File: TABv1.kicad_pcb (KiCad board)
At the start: 4 copper layers, 90 x 45 mm, 136 parts, among them IC1 TPS630702RNMR, J10 Conn_02x03_Odd_Even, J2 Conn_01x03_Socket, J3 Conn_01x03_Socket, J4 Conn_Coaxial, J5 Conn_02x06_Counter_Clockwise, J7 503398-1892, J8 1053141104, J9 Conn_02x03_Odd_Even, Q1 MJD44H11T4G, Q10 PJM09P30DF, Q11 PJM09P30DF, Q12 PJM09P30DF, Q2 DMN2040U, Q3 DMN2040U, Q4 BC817-25,215, Q5 DMN2040U, Q6 DMN2040U, Q7 DMN2040U, SW1 BOOTSEL, SW2 RESET, U1 RP2350B-QFN80, U10 RAK3172, U11 LPS22DF, U2 W25Q128JVS, U4 LSM6DSV80XTR, U5 LSM6DSV80XTR, U7 LM334M, U8 LIS2MDL, Y1 12MHz

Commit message: Tentativo di Sbroglio
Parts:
- removed FPC1: WL0540013-120R-001, easyeda2kicad:CONN-SMD_12P-WL0540013-120R-001
- removed the J5 at (87.6, 47.2)
- removed the J5 at (122.9, 47.2)
- added H5: MountingHole, MountingHole:MountingHole_3.2mm_M3, F.Cu at (131.0, 74.0)
- added H6: MountingHole, MountingHole:MountingHole_3.2mm_M3, F.Cu at (86.5, 38.0)
- added J11: Conn_02x06_Counter_Clockwise, Connector_PinHeader_2.54mm:PinHeader_2x06_P2.54mm_Vertical, B.Cu at (87.6, 47.2)
- added J6: Conn_02x06_Counter_Clockwise, Connector_PinHeader_2.54mm:PinHeader_2x06_P2.54mm_Vertical, B.Cu at (122.9, 47.2)
- BT1, C37, D8, JP1, R26, R39, R9: moved to F.Cu
- C10, C11, C12, C15, C5, C9, D5, D6, D7, J7, R7, SW1, SW2, USB1: moved to B.Cu
- moved R39 141.3 mm to (22.3, 133.1), turned to 0 degrees
- moved C37 138.9 mm to (22.3, 130.6)
- moved D8 137.3 mm to (26.7, 130.6), turned to 0 degrees
- moved BT1 135.5 mm to (29.4, 125.1), turned to 0 degrees
- moved JP1 128.3 mm to (31.1, 131.1), turned to 0 degrees
- moved R9 84.3 mm to (126.3, 60.3), turned to 0 degrees
- moved R26 82.8 mm to (126.3, 58.7), turned to 0 degrees
- moved G*** 63.2 mm to (174.4, 88.9)
- moved D10 62.8 mm to (38.8, 106.0)
- moved D11 62.8 mm to (38.8, 107.7)
- moved D9 62.8 mm to (38.8, 104.2)
- moved RN1 62.8 mm to (38.1, 115.0)
- moved C39 56.3 mm to (66.1, 104.7)
- moved C40 56.3 mm to (66.1, 103.2)
- moved C5 26.2 mm to (114.6, 59.6), turned to 180 degrees
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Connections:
- J7 pad 3: Net-(J7-CMD) -> /microSD/_CMD
- J7 pad 5: Net-(J7-CLK) -> /microSD/_CLK
- J7 pad 7: Net-(J7-DAT0) -> /microSD/_DAT0
- RN6 pad 1: Net-(J7-CMD) -> unconnected-(RN6-R1.1-Pad1)
- RN6 pad 2: unconnected-(RN6-R2.1-Pad2) -> /microSD/_CMD
- RN6 pad 7: unconnected-(RN6-R2.2-Pad7) -> +3V3
- RN7 pad 1: /microSD/_DAT3 -> unconnected-(RN7-R1.1-Pad1)
- RN7 pad 2: unconnected-(RN7-R2.1-Pad2) -> /SD_DAT1
- RN7 pad 3: Net-(J7-CMD) -> /SD_DAT0
- RN7 pad 4: /microSD/_DAT2 -> /SD_CLK
- RN7 pad 5: /SD_DAT2 -> /microSD/_CLK
- RN7 pad 6: /SD_CMD -> /microSD/_DAT0
- RN7 pad 7: unconnected-(RN7-R2.2-Pad7) -> /microSD/_DAT1
- RN7 pad 8: /SD_DAT3 -> unconnected-(RN7-R1.2-Pad8)
- RN8 pad 1: /microSD/_DAT1 -> +3V3
- RN8 pad 2: unconnected-(RN8-R2.1-Pad2) -> +3V3
- RN8 pad 3: Net-(J7-DAT0) -> +3V3
- RN8 pad 4: Net-(J7-CLK) -> +3V3
- RN8 pad 5: +3V3 -> /microSD/_DAT1
- RN8 pad 6: +3V3 -> /microSD/_DAT0
- RN8 pad 7: unconnected-(RN8-R2.2-Pad7) -> /microSD/_CLK
- RN8 pad 8: +3V3 -> unconnected-(RN8-R1.2-Pad8)
- RN9 pad 1: /microSD/_DAT1 -> /SD_CMD
- RN9 pad 2: Net-(J7-CLK) -> /SD_DAT3
- RN9 pad 3: unconnected-(RN9-R3.1-Pad3) -> /SD_DAT2
- RN9 pad 4: Net-(J7-DAT0) -> unconnected-(RN9-R4.1-Pad4)
- RN9 pad 5: /SD_DAT0 -> unconnected-(RN9-R4.2-Pad5)
- RN9 pad 6: unconnected-(RN9-R3.2-Pad6) -> /microSD/_DAT2
- RN9 pad 7: /SD_CLK -> /microSD/_DAT3
- RN9 pad 8: /SD_DAT1 -> /microSD/_CMD
- U1 pad 33: Net-(U1-SWCLK) -> /SWDCLK
- U1 pad 34: Net-(U1-SWDIO) -> /SWDIO
- U1 pad 48: unconnected-(U1-GPIO39-Pad48) -> /GPIO39
- U1 pad 56: unconnected-(U1-GPIO45_ADC5-Pad56) -> /GPIO45
- U1 pad 57: unconnected-(U1-GPIO46_ADC6-Pad57) -> /GPIO46
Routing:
- net VUSB: track 0.00 -> 93.3 mm, vias 0 -> 1
- net /BATT_SENSE: track 1.55 -> 87.5 mm, vias 0 -> 4
- net +3V3: track 19.6 -> 83.7 mm, vias 7 -> 32
- net /SPI1.CK: track 0.00 -> 63.4 mm, vias 0 -> 5
- net /PYRO_FIRE_1: track 0.00 -> 62.8 mm, vias 0 -> 2
- net /SPI1.TX: track 0.00 -> 61.0 mm, vias 0 -> 4
- net /PWM1: track 0.00 -> 59.4 mm, vias 0 -> 1
- net /PWM2: track 0.00 -> 57.0 mm, vias 0 -> 1
- net /SPI1.RX: track 0.00 -> 56.4 mm, vias 0 -> 4
- net /PYRO_SENSE: track 1.60 -> 57.9 mm, vias 0 -> 4
- net /PYRO_FIRE_2: track 0.00 -> 54.7 mm, vias 0 -> 2
- net /PWM3: track 0.00 -> 54.5 mm, vias 0 -> 3
- net /PWM4: track 0.00 -> 52.5 mm, vias 0 -> 3
- net /PYRO_FIRE_3: track 0.00 -> 52.0 mm, vias 0 -> 4
- net /MAG_CS: track 0.00 -> 47.5 mm, vias 0 -> 2
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- removed copper zone on F.Cu, net +1V1
- removed copper zone on F.Cu, net /LX
- removed copper zone on F.Cu, net GND
- removed copper zone on In2.Cu, net GND
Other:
- board text added: "Convertire in un singolo onnettore da 6"
- board text added: "REV 2.0"
- board text removed: "BOOTSEL"
- board text removed: "IO"
- board text removed: "RESET"
- board text removed: "REV 1.1"
- board text removed: "RX"
- board text removed: "TX"

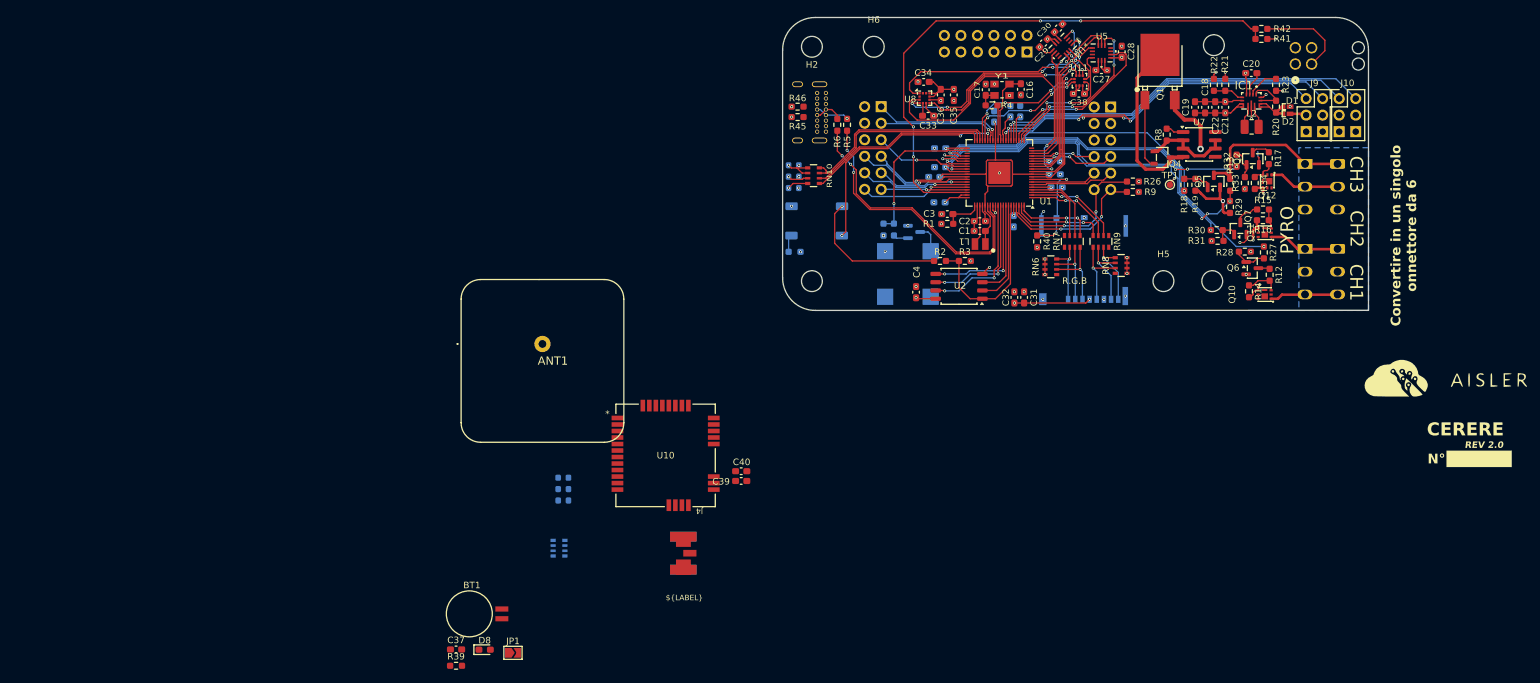
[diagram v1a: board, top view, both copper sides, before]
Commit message: connessione 1v1 sotto il rp2350 come la fa raspberry pi, tracce con l impedenza corretta sulla usb, aggiunto collegamenti mancanti e un pò di drc
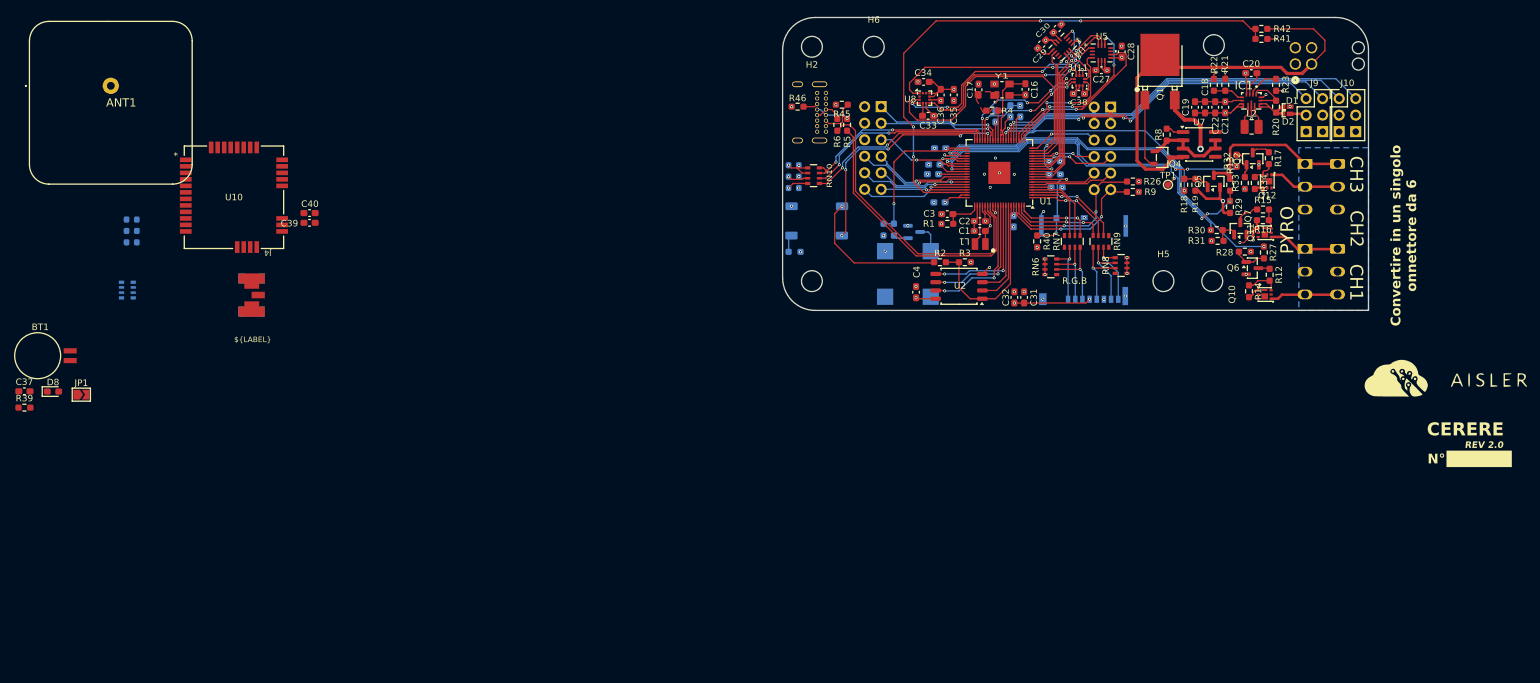
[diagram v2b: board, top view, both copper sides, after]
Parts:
- removed J5: Conn_02x06_Counter_Clockwise, Connector_PinHeader_2.54mm:PinHeader_2x06_P2.54mm_Vertical
- moved C39 77.3 mm to (-0.17, 65.0)
- moved C40 77.3 mm to (-0.17, 63.5)
- moved ANT1 77.3 mm to (-30.7, 44.0)
- moved BT1 77.3 mm to (-36.9, 85.5)
- moved C37 77.3 mm to (-44.0, 90.9)
- moved D10 77.3 mm to (-27.5, 66.3)
- moved D11 77.3 mm to (-27.5, 68.0)
- moved D8 77.3 mm to (-39.6, 91.0)
- moved D9 77.3 mm to (-27.5, 64.5)
- moved J4 77.3 mm to (-11.1, 76.1)
- moved JP1 77.3 mm to (-35.2, 91.4)
- moved R39 77.3 mm to (-44.0, 93.4)
- moved RN1 77.3 mm to (-28.2, 75.4)
- moved U10 77.3 mm to (-11.8, 61.1)
- moved R45 7.06 mm to (81.6, 46.9)
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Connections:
- J6 pad 1: unconnected-(J6-Pin_1-Pad1) -> /PWM4
- J6 pad 2: unconnected-(J6-Pin_2-Pad2) -> /PWM1
- J6 pad 3: unconnected-(J6-Pin_3-Pad3) -> /PWM2
- J6 pad 4: unconnected-(J6-Pin_4-Pad4) -> /PWM3
- J6 pad 6: unconnected-(J6-Pin_6-Pad6) -> /GPIO20
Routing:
- net +BATT: track 43.2 -> 68.3 mm
- net /GPIO20: track 0.00 -> 10.9 mm, vias 0 -> 1
- net Net-(USB1-CC1): track 0.00 -> 5.82 mm
- net GND: track 60.1 -> 65.0 mm, vias 57 -> 58
- net +1V1: track 44.1 -> 40.4 mm, vias 3 -> 8
- net Net-(C17-Pad2): track 2.90 -> 0.00 mm
- net Net-(U1-USB_DM): track 42.9 -> 45.6 mm, vias 2 -> 0
- net Net-(USB1-CC2): track 0.00 -> 2.26 mm
- net +3V3: track 83.7 -> 85.2 mm
- net /PWM1: track 59.4 -> 60.5 mm
- net /XIN: track 10.7 -> 11.7 mm
- net /XOUT: track 5.46 -> 4.66 mm
- net Net-(U1-USB_DP): track 42.9 -> 43.6 mm, vias 2 -> 0
- net /SPI1.RX: track 56.4 -> 57.1 mm
- net /MAG_CS: track 47.5 -> 48.2 mm
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- added copper zone on In2.Cu, net +1V1
- added copper zone on F.Cu, net Net-(C17-Pad2)

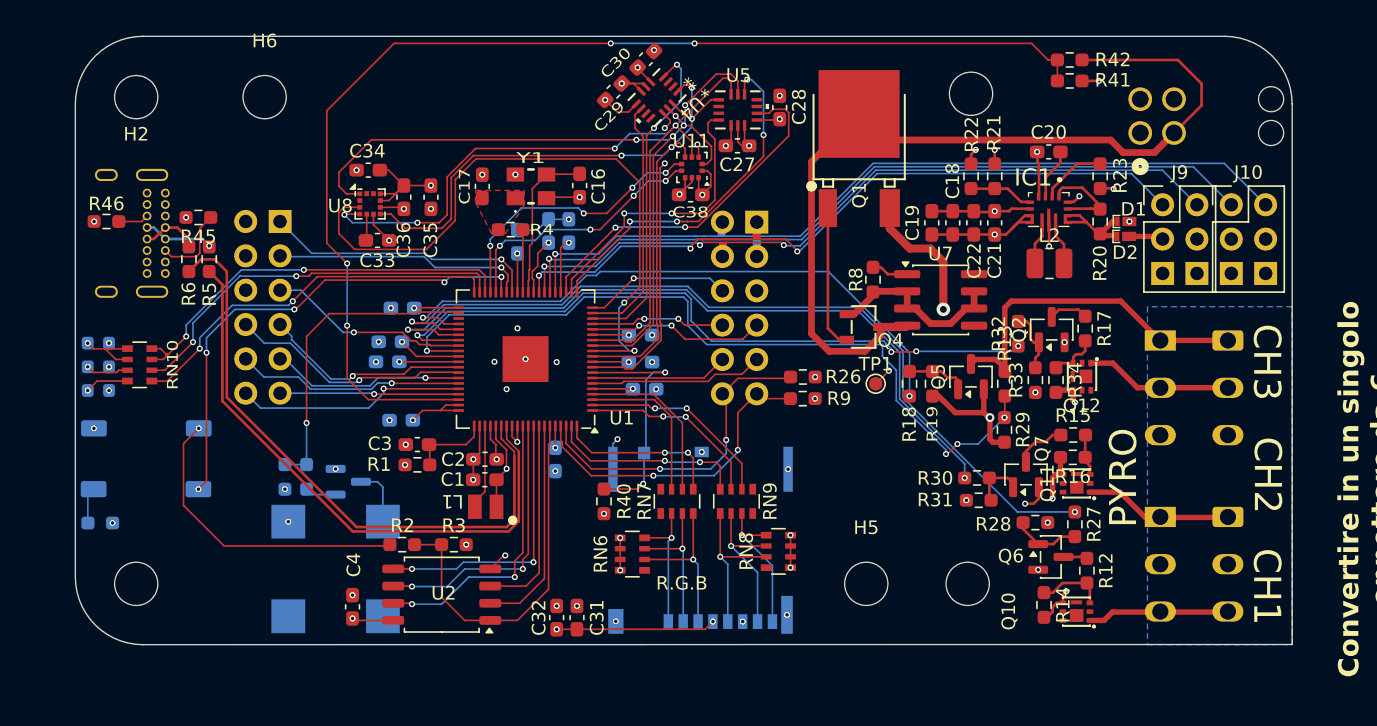
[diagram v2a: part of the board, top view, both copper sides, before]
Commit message: fixed the connectors, rearranged sensors and fixed a bit the silkscreen
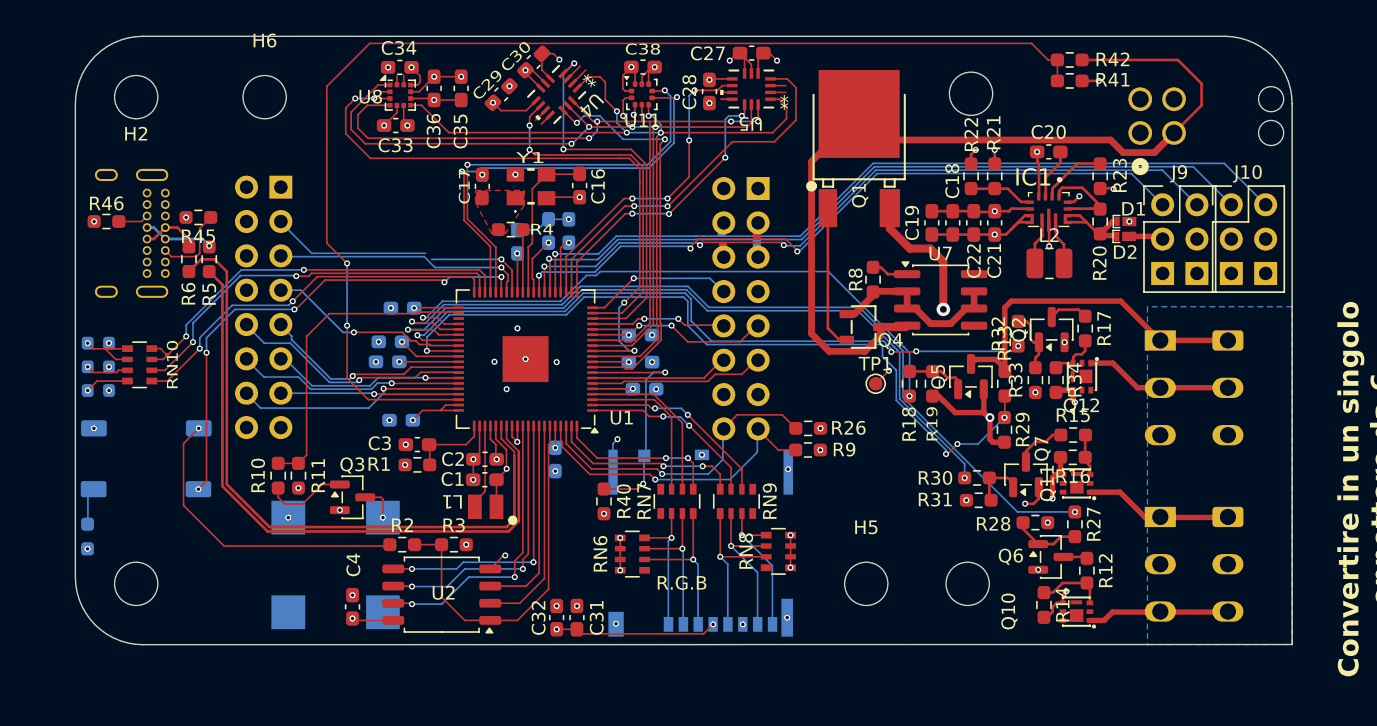
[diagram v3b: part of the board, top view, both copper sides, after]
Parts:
- removed J11: Conn_02x06_Counter_Clockwise, Connector_PinHeader_2.54mm:PinHeader_2x06_P2.54mm_Vertical
- added J5: Conn_02x08_Odd_Even, Connector_PinHeader_2.54mm:PinHeader_2x08_P2.54mm_Vertical, B.Cu at (123.0, 44.8)
- J6: value Conn_02x06_Counter_Clockwise -> Conn_02x08_Odd_Even; footprint Connector_PinHeader_2.54mm:PinHeader_2x06_P2.54mm_Vertical -> Connector_PinHeader_2.54mm:PinHeader_2x08_P2.54mm_Vertical
- Q3, R10, R11: moved to F.Cu
- moved J6 35.3 mm to (87.7, 44.7)
- moved C38 10.1 mm to (114.5, 35.8), turned to 0 degrees
- moved C33 8.61 mm to (96.2, 40.1)
- moved C35 8.36 mm to (101.0, 37.4)
- moved C36 8.36 mm to (99.0, 37.4)
- moved U8 8.36 mm to (96.5, 37.9)
- moved C29 8.30 mm to (104.0, 37.8)
- moved C30 8.30 mm to (106.4, 35.4), turned to 45 degrees
- moved C34 7.95 mm to (96.5, 35.8)
- moved U4 7.43 mm to (108.1, 37.8)
- moved C27 6.94 mm to (122.5, 34.7), turned to 0 degrees
- moved U11 6.55 mm to (114.4, 37.8), turned to 0 degrees
- moved C28 5.33 mm to (119.4, 37.6), turned to 90 degrees
- moved R26 3.82 mm to (126.7, 62.5)
- moved R9 3.82 mm to (126.7, 64.1)
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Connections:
- J6 pad 1: /PWM4 -> +3V3
- J6 pad 10: HIL_RX -> /GPIO42
- J6 pad 11: /SDA_RADIO -> /GPIO43
- J6 pad 12: /SCL_RADIO -> /GPIO44
- J6 pad 2: /PWM1 -> +3V3
- J6 pad 3: /PWM2 -> /SWDCLK
- J6 pad 4: /PWM3 -> GND
- J6 pad 5: unconnected-(J6-Pin_5-Pad5) -> /SWDIO
- J6 pad 6: /GPIO20 -> GND
- J6 pad 7: /RX_GPS -> /GPIO39
- J6 pad 8: /TX_GPS -> GND
- J6 pad 9: HIL_TX -> /GPIO41
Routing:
- net /BARO_INT: track 19.3 -> 31.0 mm, vias 4 -> 2
- net /BARO_CS: track 20.7 -> 31.7 mm, vias 4 -> 2
- net /IMU45_INT2: track 18.4 -> 26.2 mm, vias 0 -> 2
- net /IMU45_CS: track 23.3 -> 29.9 mm
- net /IMU_INT1: track 21.4 -> 27.9 mm
- net /IMU_CS: track 26.3 -> 21.5 mm
- net /SPI1.RX: track 57.1 -> 61.7 mm
- net /IMU45_INT1: track 24.4 -> 28.9 mm
- net Net-(U1-USB_DM): track 45.6 -> 49.4 mm
- net Net-(Q3-G): track 2.32 -> 6.06 mm
- net Net-(U1-USB_DP): track 43.6 -> 47.3 mm
- net /SPI1.TX: track 61.5 -> 58.8 mm
- net /IMU_INT2: track 26.2 -> 23.7 mm, vias 2 -> 4
- net GND: track 65.0 -> 67.3 mm, vias 58 -> 57
- net +3V3: track 85.2 -> 87.2 mm, vias 32 -> 34
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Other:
- board text added: "16"
- board text added: "17"
- board text added: "20"
- board text added: "24"
- board text added: "25"
- board text added: "26"
- board text added: "27"
- board text added: "39"
- board text added: "3V3"
- board text added: "41"
- board text added: "42"
- board text added: "43"
- board text added: "44"
- board text added: "45"
- board text added: "46"
- board text added: "8"
- board text added: "9"
- board text added: "BATT"
- board text added: "BOOT"
- board text added: "RESET"
- board text added: "SCL"
- board text added: "SDA"
- board text added: "SERVO"
- board text added: "SWDCK"
- board text added: "SWDIO"

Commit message: small fixes, started working on the backpack
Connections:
- J6 pad 4: GND -> PPS
- J6 pad 6: GND -> BOOTSEL
- J6 pad 8: GND -> /RESET
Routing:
- net PPS: track 0.00 -> 27.1 mm, vias 0 -> 2
- net BOOTSEL: track 22.7 -> 37.8 mm, vias 1 -> 2
- net /RESET: track 36.4 -> 40.5 mm
- net /PYRO_SENSE: track 57.9 -> 58.6 mm
- net /PYRO_FIRE_3: track 52.0 -> 52.7 mm
- net /PYRO_FIRE_1: track 62.8 -> 63.5 mm
- net /PYRO_FIRE_2: track 54.7 -> 55.3 mm
- net /SWDCLK: track 19.6 -> 20.3 mm
- net /PYRO_ENABLE: track 45.9 -> 46.5 mm

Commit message: aiuto
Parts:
- removed ANT1: AANI-PP-0055, antenna_GPS:AANIPP0055
- removed BT1: Battery_Cell, Battery:BatteryHolder_Seiko_MS621F
- removed C37, C40: 100nF, Capacitor_SMD:C_0603_1608Metric_Pad1.08x0.95mm_HandSolder
- removed C39: 10nF, Capacitor_SMD:C_0603_1608Metric_Pad1.08x0.95mm_HandSolder
- removed D10: GREEN, LED_SMD:LED_0603_1608Metric
- removed D11: RED, LED_SMD:LED_0603_1608Metric
- removed D8: D_Schottky_Small, Diode_SMD:D_0603_1608Metric_Pad1.05x0.95mm_HandSolder
- removed D9: BLUE, LED_SMD:LED_0603_1608Metric
- removed J4: Conn_Coaxial, sma_connector:SMA_EDGE__UFL
- removed JP1: SolderJumper_2_Open, Jumper:SolderJumper-2_P1.3mm_Open_TrianglePad1.0x1.5mm
- removed R39: 47k, Resistor_SMD:R_0603_1608Metric_Pad0.98x0.95mm_HandSolder
- removed RN1: 220, Resistor_SMD:R_Array_Convex_4x0603
- removed TP1: TestPoint, TestPoint:TestPoint_Pad_D1.0mm
- removed U10: RAK3172, ul_RAK3172:RAK3172_RAK
- moved G*** 90.0 mm to (92.8, 50.9), turned to -90 degrees
- moved G*** 34.4 mm to (135.5, 54.2), turned to -90 degrees
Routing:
- net Net-(U9-PRG): track 1.24 -> 0.00 mm, vias 1 -> 0
- net Net-(U8-C1): vias 1 -> 0
- net +1V1: vias 8 -> 4
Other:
- board text removed: "CLK"
- board text removed: "CPU"
- board text removed: "DIO"
- board text removed: "RADIO"

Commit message: ficato connetotore wagoi se negro
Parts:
- removed J2, J3: Conn_01x03_Socket, TerminalBlock_WAGO:TerminalBlock_WAGO_2601-1103_1x03_P3.50mm_Horizontal
- added J11: Conn_01x06_Pin, TerminalBlock_WAGO:TerminalBlock_WAGO_2601-1106_1x06_P3.50mm_Horizontal, F.Cu at (157.5, 74.5)
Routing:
- net /Pyro/PYRO2: track 11.0 -> 10.0 mm
- net /Pyro/PYRO_LOW: track 25.7 -> 26.6 mm
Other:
- board text removed: "Convertire in un singolo onnettore da 6"

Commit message: Ordered
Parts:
- moved J11 0.33 mm to (157.8, 74.5)
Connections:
- Q10 pad 2: unconnected-(Q10-D-Pad2) -> /Pyro/PYRO1
- Q10 pad 5: unconnected-(Q10-D-Pad5) -> /Pyro/PYRO1
- Q10 pad 6: unconnected-(Q10-D-Pad6) -> /Pyro/PYRO1
- Q10 pad 7: unconnected-(Q10-D-Pad7) -> /Pyro/PYRO1
- Q10 pad 8: unconnected-(Q10-S-Pad8) -> /Pyro/PYRO_HIGH
- Q11 pad 2: unconnected-(Q11-D-Pad2) -> /Pyro/PYRO2
- Q11 pad 5: unconnected-(Q11-D-Pad5) -> /Pyro/PYRO2
- Q11 pad 6: unconnected-(Q11-D-Pad6) -> /Pyro/PYRO2
- Q11 pad 7: unconnected-(Q11-D-Pad7) -> /Pyro/PYRO2
- Q11 pad 8: unconnected-(Q11-S-Pad8) -> /Pyro/PYRO_HIGH
- Q12 pad 2: unconnected-(Q12-D-Pad2) -> /Pyro/PYRO3
- Q12 pad 5: unconnected-(Q12-D-Pad5) -> /Pyro/PYRO3
- Q12 pad 6: unconnected-(Q12-D-Pad6) -> /Pyro/PYRO3
- Q12 pad 7: unconnected-(Q12-D-Pad7) -> /Pyro/PYRO3
- Q12 pad 8: unconnected-(Q12-S-Pad8) -> /Pyro/PYRO_HIGH
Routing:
- net /Pyro/PYRO3: track 11.0 -> 22.6 mm
- net /Pyro/PYRO1: track 10.8 -> 18.9 mm
- net /Pyro/PYRO2: track 10.0 -> 17.9 mm
- net /Pyro/PYRO_HIGH: track 19.1 -> 23.1 mm
- net /Pyro/PYRO_LOW: track 26.6 -> 27.2 mm
- net GND: vias 57 -> 59
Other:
- board text added: "R G B"
